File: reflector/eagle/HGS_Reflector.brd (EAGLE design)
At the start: 100 x 100 mm, 24 parts, among them J1 U.FL, U3 LP2985XX-N

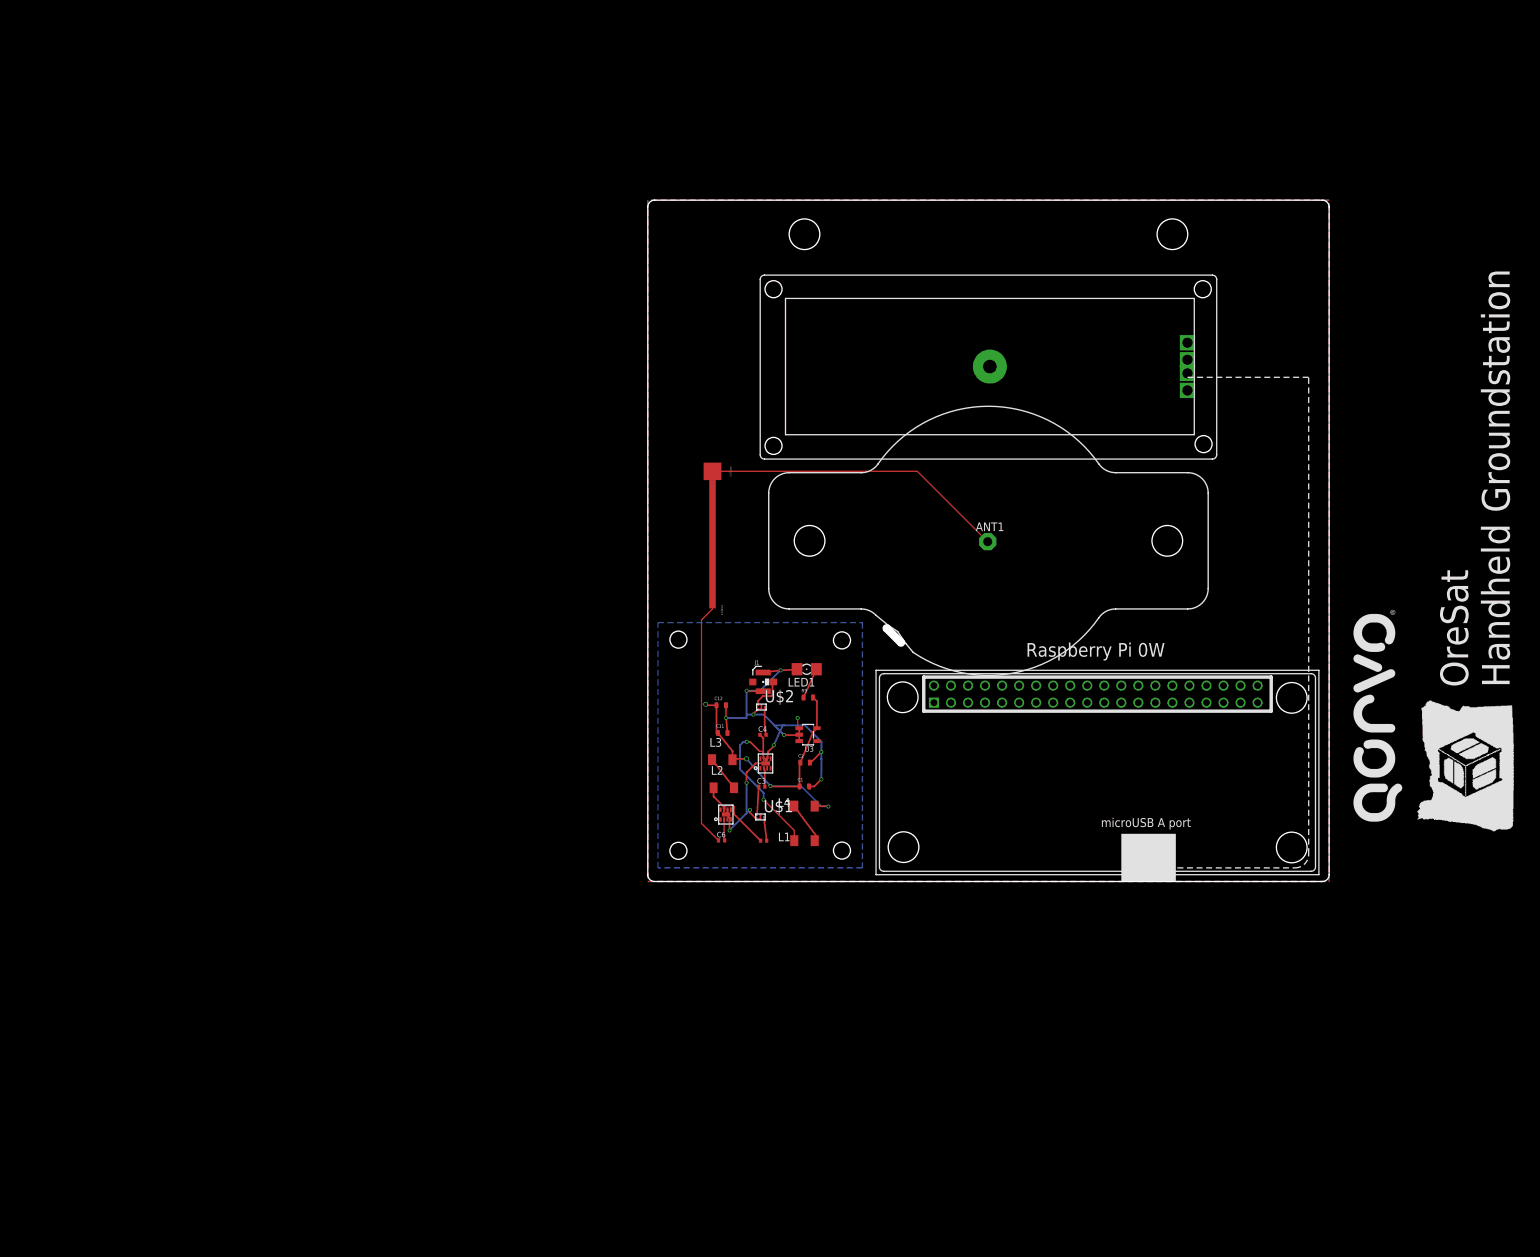
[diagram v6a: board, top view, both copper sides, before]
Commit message: Since the team working on HGS decided to switch from a 2 layer board to a 4 layer board, I began laying out the HGS parts on a new board with 4 layers. Currently, I have a number of questions regarding the layout to go over at the 11/29 structure meeting.
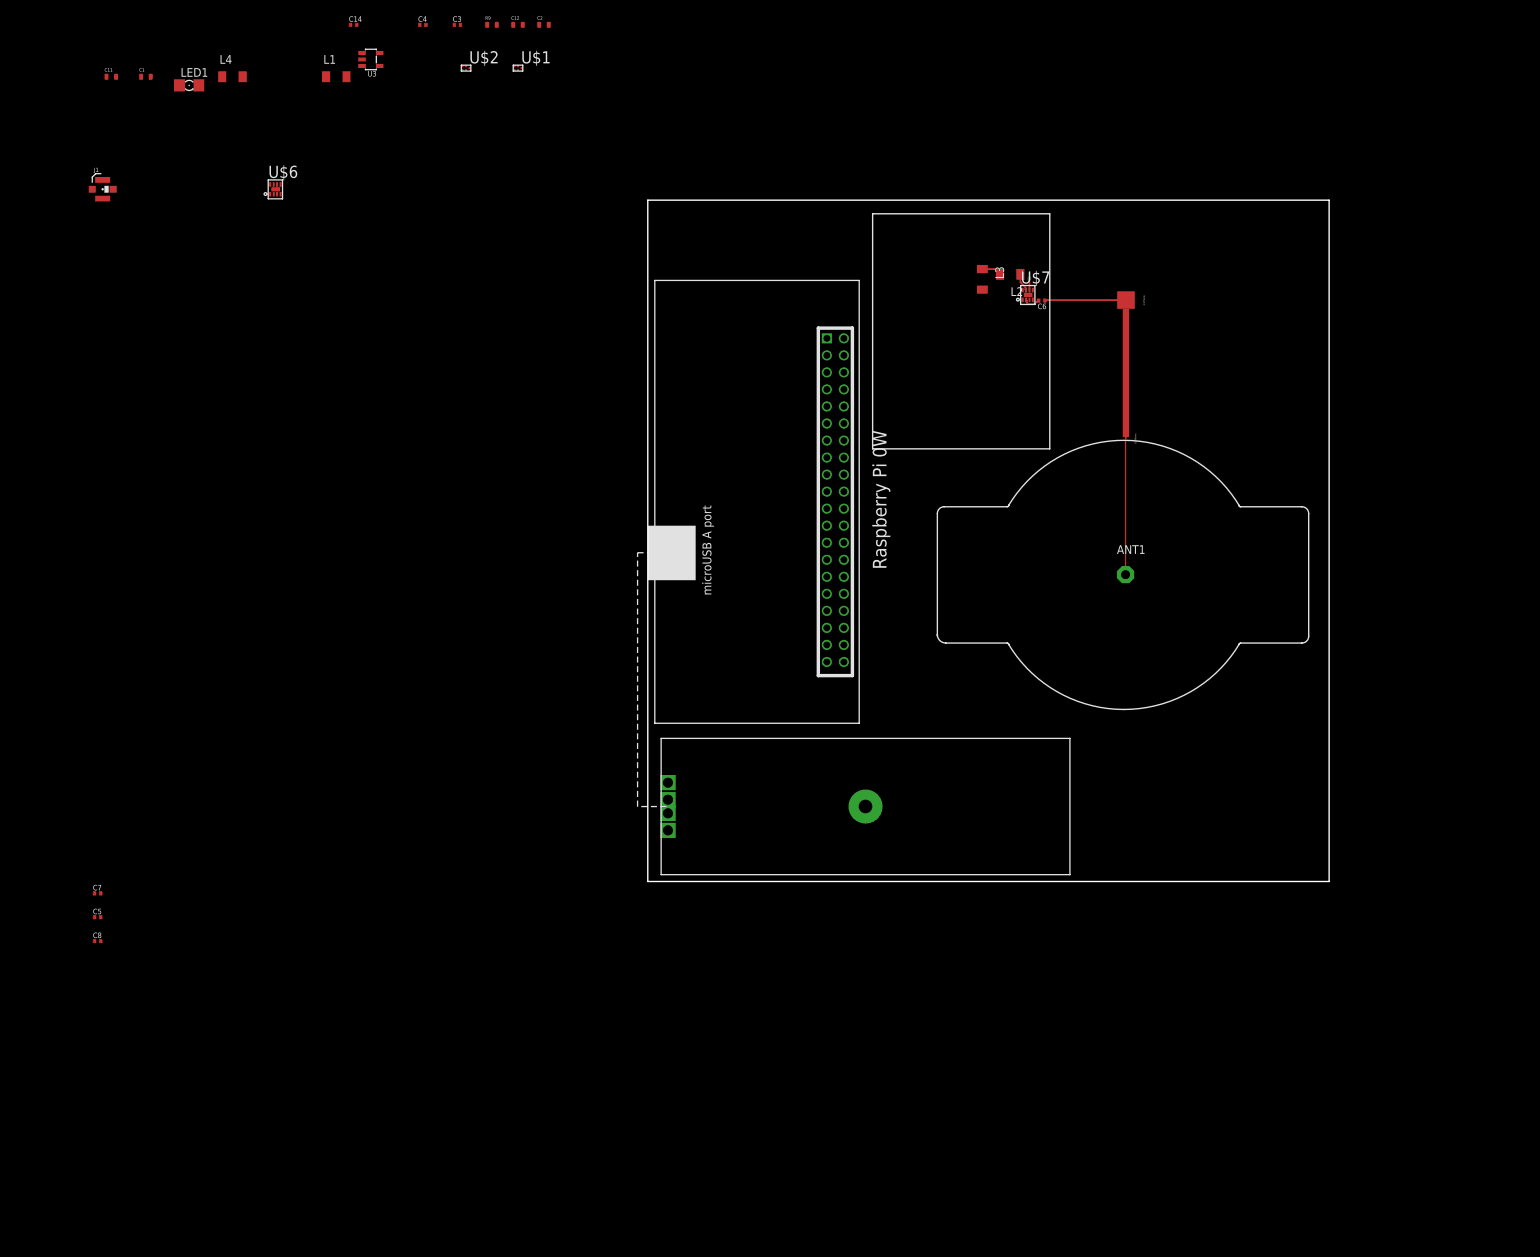
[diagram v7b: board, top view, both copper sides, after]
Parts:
- added C5: 10 nF, oresat-rcl:.0402-C-NOSILK
- added C7: 1 uF, oresat-rcl:.0402-C-NOSILK
- added C8: 2.2 uF, oresat-rcl:.0402-C-NOSILK
- moved C1 142.1 mm to (-73.7, 118.1)
- moved L4 136.0 mm to (-61.0, 118.1)
- moved C14 134.0 mm to (-43.2, 125.7)
- moved C11 131.6 mm to (-78.7, 118.1)
- moved L1 131.5 mm to (-45.7, 118.1)
- moved LED1 124.7 mm to (-67.3, 116.8), turned to 0 degrees
- moved J1 120.9 mm to (-80.0, 101.6)
- moved C3 120.4 mm to (-27.9, 125.7)
- moved U3 118.1 mm to (-40.6, 120.7)
- moved C4 115.5 mm to (-33.0, 125.7)
- moved U$1 115.5 mm to (-19.1, 119.4)
- moved C2 114.9 mm to (-15.2, 125.7)
- moved U$6 110.8 mm to (-54.6, 101.6)
- moved R9 109.1 mm to (-22.9, 125.7)
- moved C12 104.2 mm to (-19.1, 125.7)
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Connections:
- removed net N$12: ANT1.1, U$3.P$1
- new net N$2: ANT1.1, U$3.P$2
- net 3.3V: now also C8.1
- net 5V: now also C7.2
- net GND: now also C5.2, C7.1, C8.2
- net N$1: now also C5.1
- net N$9: now also U$3.P$1; no longer U$3.P$2
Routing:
- net GND: track 82.6 -> 1.71 mm, vias 11 -> 1
- net 3.3V: track 48.2 -> 0.00 mm, vias 4 -> 0
- net N$12: track 44.7 -> 0.00 mm
- net N$13: track 25.6 -> 0.00 mm, vias 2 -> 0
- net N$9: track 35.7 -> 11.9 mm
- net N$2: track 0.00 -> 20.2 mm
- net N$16: track 12.4 -> 2.65 mm
- net N$14: track 6.37 -> 0.00 mm
- net N$5: track 5.08 -> 0.00 mm
- net N$10: track 4.56 -> 0.00 mm
- net N$4: track 4.16 -> 0.00 mm
- net N$3: track 4.10 -> 0.00 mm
- net N$6: track 3.50 -> 0.00 mm
- net 5V: track 3.49 -> 0.00 mm, vias 1 -> 0
- net N$8: track 2.73 -> 0.00 mm
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- removed copper zone on layer 16, net GND
- removed copper zone on layer 1, net GND1
- removed copper zone on layer 15, net GND1
- removed copper zone on layer 16, net GND1
- removed copper zone on layer 2, net GND1
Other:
- outline, holes or cut-outs redrawn
- board text removed: "OreSat Handheld Groundstation"

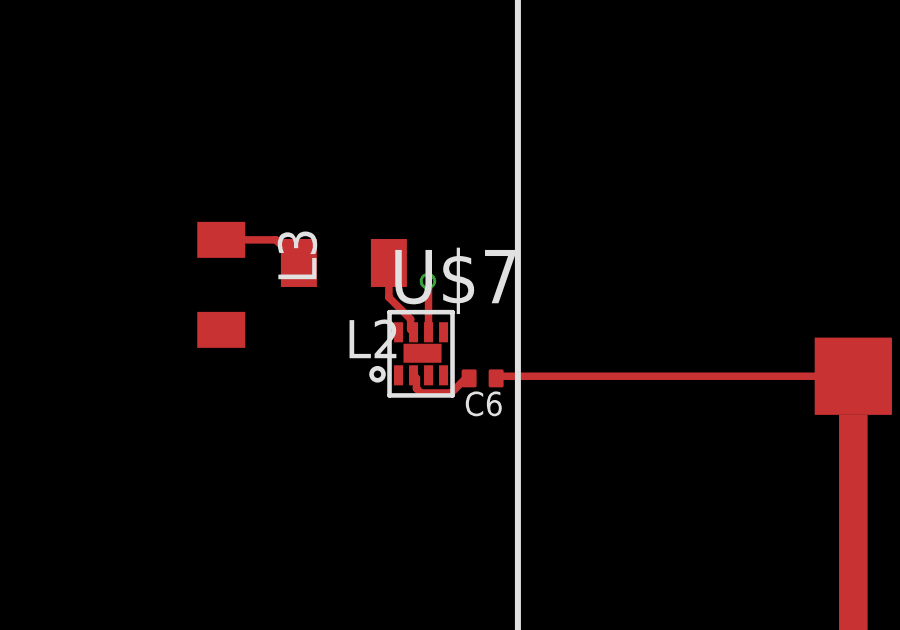
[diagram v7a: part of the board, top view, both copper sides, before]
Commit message: I added a ground plane to the new HGS board layout.
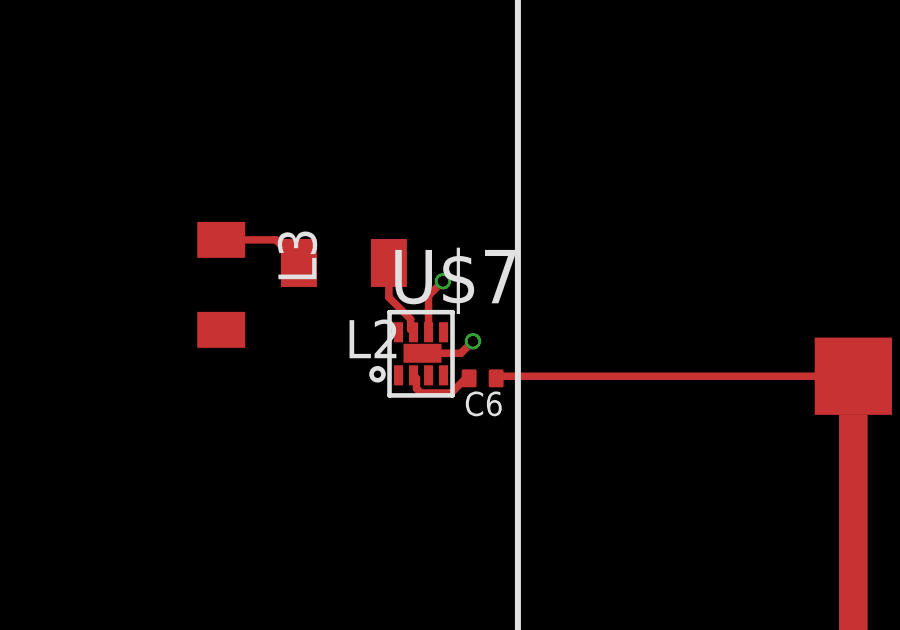
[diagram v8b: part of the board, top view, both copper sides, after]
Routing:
- net GND: track 1.71 -> 3.74 mm, vias 1 -> 2
- added copper zone on layer 15, net GND
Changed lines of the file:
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@@
 <contactref element="C8" pad="2"/>
 <contactref element="C5" pad="2"/>
-<wire x1="56.02" y1="86.8" x2="56.02" y2="88.48" width="0.25" layer="1"/>
-<wire x1="56.02" y1="88.48" x2="56" y2="88.5" width="0.25" layer="1"/>
-<via x="56" y="88.5" extent="1-16" drill="0.35"/>
+<polygon width="1.5" layer="15" spacing="1" pour="hatch" isolate="2.54" rank="2">
+<vertex x="1" y="23"/>
+<vertex x="1" y="99"/>
+<vertex x="60" y="99"/>
+<vertex x="60" y="23"/>
+</polygon>
+<wire x1="56.02" y1="86.8" x2="56.02" y2="88.02" width="0.25" layer="1"/>
+<wire x1="56.02" y1="88.02" x2="56.5" y2="88.5" width="0.25" layer="1"/>
+<via x="56.5" y="88.5" extent="1-16" drill="0.35"/>
+<wire x1="55.82" y1="86.1" x2="57.1" y2="86.1" width="0.25" layer="1"/>
+<wire x1="57.1" y1="86.1" x2="57.5" y2="86.5" width="0.25" layer="1"/>
+<via x="57.5" y="86.5" extent="1-16" drill="0.35"/>
 <wire x1="55.82" y1="86.1" x2="56.02" y2="86.8" width="0" layer="19" extent="1-1"/>
-<wire x1="-14.54" y1="125.73" x2="56" y2="88.5" width="0" layer="19" extent="1-1"/>
+<wire x1="-14.54" y1="125.73" x2="56.5" y2="88.5" width="0" layer="19" extent="1-1"/>
 <wire x1="-18.35" y1="125.73" x2="-14.54" y2="125.73" width="0" layer="19" extent="1-1"/>
 <wire x1="-19.05" y1="119.6655" x2="-18.35" y2="125.73" width="0" layer="19" extent="1-1"/>
@@
 <contactref element="U3" pad="5"/>
 <contactref element="C8" pad="1"/>
+<wire x1="-15.94" y1="125.73" x2="49.11" y2="86.88" width="0" layer="19" extent="1-1"/>
 <wire x1="-19.75" y1="125.73" x2="-15.94" y2="125.73" width="0" layer="19" extent="1-1"/>
 <wire x1="-22.16" y1="125.73" x2="-19.75" y2="125.73" width="0" layer="19" extent="1-1"/>
 <wire x1="-39.34" y1="121.6" x2="-22.16" y2="125.73" width="0" layer="19" extent="1-1"/>
-<wire x1="49.11" y1="86.88" x2="-39.34" y2="121.6" width="0" layer="19" extent="1-1"/>
-<wire x1="-59.46" y1="118.11" x2="49.11" y2="86.88" width="0" layer="19" extent="1-1"/>
+<wire x1="-59.46" y1="118.11" x2="-39.34" y2="121.6" width="0" layer="19" extent="1-1"/>
 <wire x1="-74.36" y1="118.11" x2="-59.46" y2="118.11" width="0" layer="19" extent="1-1"/>
 <wire x1="-79.44" y1="118.11" x2="-74.36" y2="118.11" width="0" layer="19" extent="1-1"/>
